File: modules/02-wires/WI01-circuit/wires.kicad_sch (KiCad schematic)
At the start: 24 parts, among them J1 MODULE Connector, SW1 SW_SPST, SW2 SW_SPST, SW3 SW_SPST, SW4 SW_SPST, SW5 SW_SPST, SW6 SW_SPST

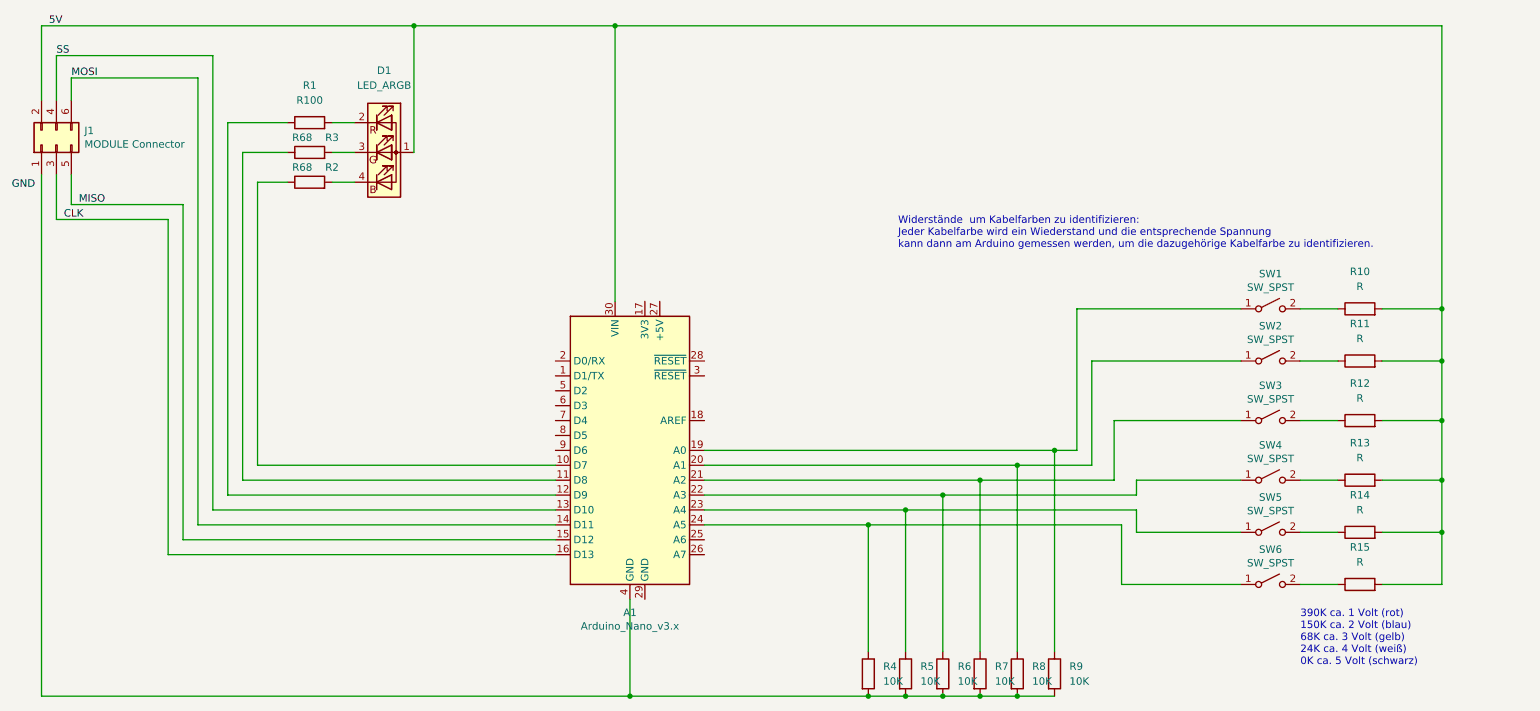
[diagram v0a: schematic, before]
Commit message: cleanup circuit
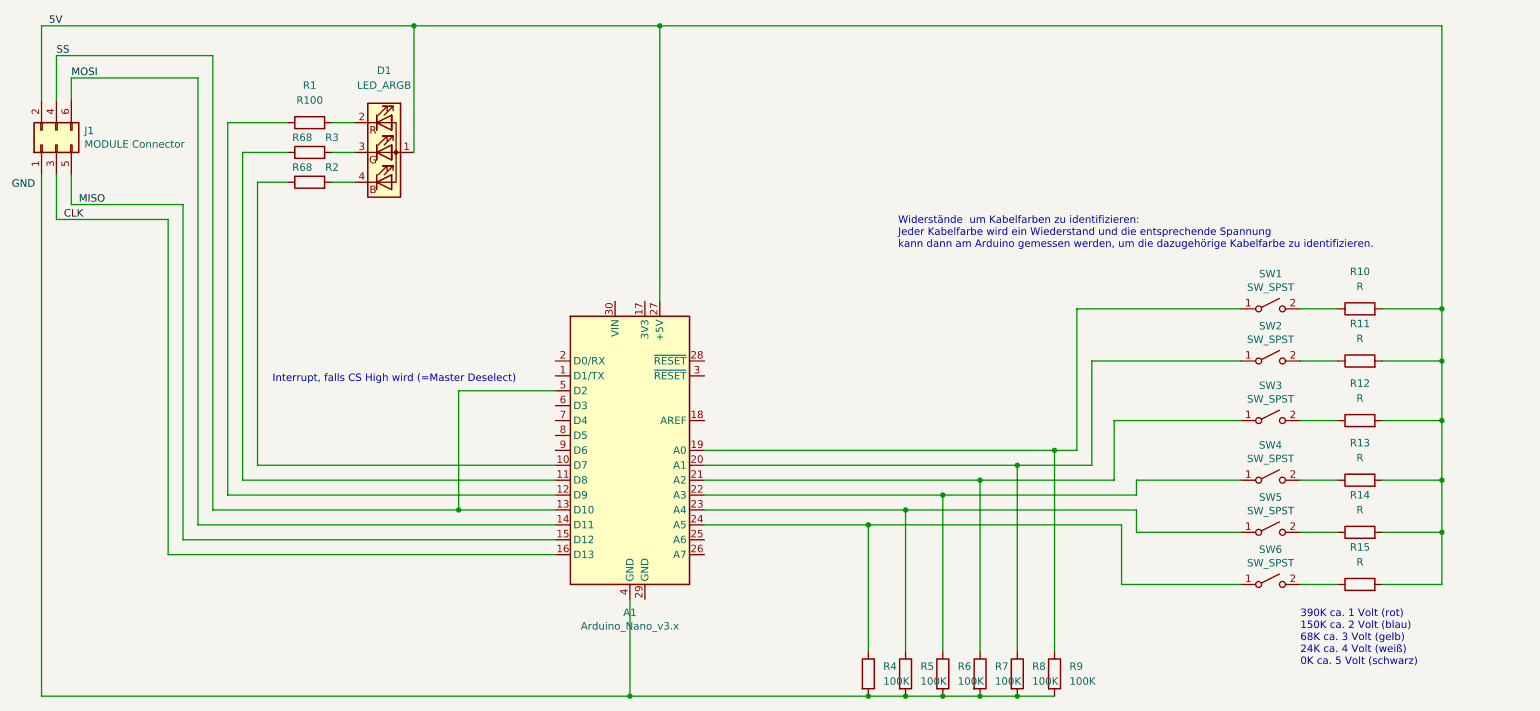
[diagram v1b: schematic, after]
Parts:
- R4, R5, R6, R7, R8, R9: value 10K -> 100K
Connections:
- net 5V: now also A1.27 (+5V); no longer A1.30 (VIN)
- net SS: now also A1.5 (D2)
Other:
- note added: "Interrupt, falls CS High wird (=Master Deselect)"
- title: (none) -> Schaltplan Modul Wires (02)
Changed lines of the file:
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@@
 (kicad_sch (version 20211123) (generator eeschema)
   (paper "A4")
+  (title_block
+    (title "Schaltplan Modul Wires (02)")
+    (date "14.12.2022")
+  )
   (junction (at 214.63 110.49) (diameter 0) (color 0 0 0 0)
   )
@@
   (junction (at 105.41 38.1) (diameter 0) (color 0 0 0 0)
   )
-  (junction (at 139.7 38.1) (diameter 0) (color 0 0 0 0)
-  )
   (junction (at 208.28 152.4) (diameter 0) (color 0 0 0 0)
   )
@@
   (junction (at 208.28 113.03) (diameter 0) (color 0 0 0 0)
   )
+  (junction (at 113.03 120.65) (diameter 0) (color 0 0 0 0)
+  )
   (junction (at 280.67 95.25) (diameter 0) (color 0 0 0 0)
   )
   (junction (at 182.88 152.4) (diameter 0) (color 0 0 0 0)
   )
+  (junction (at 147.32 38.1) (diameter 0) (color 0 0 0 0)
+  )
   (junction (at 189.23 152.4) (diameter 0) (color 0 0 0 0)
   )
@@
     (stroke (width 0) (type default) (color 0 0 0 0))
   )
-  (wire (pts (xy 71.12 120.65) (xy 129.54 120.65))
+  (wire (pts (xy 71.12 120.65) (xy 113.03 120.65))
     (stroke (width 0) (type default) (color 0 0 0 0))
   )
@@
     (stroke (width 0) (type default) (color 0 0 0 0))
   )
+  (wire (pts (xy 147.32 38.1) (xy 280.67 38.1))
+    (stroke (width 0) (type default) (color 0 0 0 0))
+  )
   (wire (pts (xy 280.67 86.36) (xy 280.67 95.25))
     (stroke (width 0) (type default) (color 0 0 0 0))
@@
     (stroke (width 0) (type default) (color 0 0 0 0))
   )
+  (wire (pts (xy 147.32 85.09) (xy 147.32 38.1))
+    (stroke (width 0) (type default) (color 0 0 0 0))
+  )
   (wire (pts (xy 46.99 50.8) (xy 46.99 46.99))
     (stroke (width 0) (type default) (color 0 0 0 0))
@@
     (stroke (width 0) (type default) (color 0 0 0 0))
   )
+  (wire (pts (xy 113.03 120.65) (xy 113.03 100.33))
+    (stroke (width 0) (type default) (color 0 0 0 0))
+  )
   (wire (pts (xy 142.24 152.4) (xy 142.24 135.89))
     (stroke (width 0) (type default) (color 0 0 0 0))
@@
     (stroke (width 0) (type default) (color 0 0 0 0))
   )
-  (wire (pts (xy 139.7 38.1) (xy 280.67 38.1))
-    (stroke (width 0) (type default) (color 0 0 0 0))
-  )
   (wire (pts (xy 201.93 115.57) (xy 224.79 115.57))
     (stroke (width 0) (type default) (color 0 0 0 0))
@@
     (stroke (width 0) (type default) (color 0 0 0 0))
   )
-  (wire (pts (xy 105.41 38.1) (xy 139.7 38.1))
+  (wire (pts (xy 113.03 100.33) (xy 129.54 100.33))
+    (stroke (width 0) (type default) (color 0 0 0 0))
+  )
+  (wire (pts (xy 113.03 120.65) (xy 129.54 120.65))
     (stroke (width 0) (type default) (color 0 0 0 0))
   )
@@
     (stroke (width 0) (type default) (color 0 0 0 0))
   )
+  (wire (pts (xy 105.41 38.1) (xy 147.32 38.1))
+    (stroke (width 0) (type default) (color 0 0 0 0))
+  )
   (wire (pts (xy 214.63 110.49) (xy 218.44 110.49))
     (stroke (width 0) (type default) (color 0 0 0 0))
@@
   )
   (wire (pts (xy 154.94 123.19) (xy 182.88 123.19))
-    (stroke (width 0) (type default) (color 0 0 0 0))
-  )
-  (wire (pts (xy 139.7 38.1) (xy 139.7 85.09))
     (stroke (width 0) (type default) (color 0 0 0 0))
   )
@@
   (text "390K ca. 1 Volt (rot)\n150K ca. 2 Volt (blau)\n68K ca. 3 Volt (gelb)\n24K ca. 4 Volt (weiß)\n0K ca. 5 Volt (schwarz)"
     (at 256.54 147.32 0)
+    (effects (font (size 1.27 1.27)) (justify left bottom))
+  )
+  (text "Interrupt, falls CS High wird (=Master Deselect)\n" (at 81.28 99.06 0)
     (effects (font (size 1.27 1.27)) (justify left bottom))
   )
@@
       (effects (font (size 1.27 1.27)) (justify left))
     )
-    (property "Value" "10K" (id 1) (at 210.82 149.8599 0)
+    (property "Value" "100K" (id 1) (at 210.82 149.8599 0)
       (effects (font (size 1.27 1.27)) (justify left))
     )
@@
       (effects (font (size 1.27 1.27)) (justify left))
     )
-    (property "Value" "10K" (id 1) (at 191.77 149.8599 0)
+    (property "Value" "100K" (id 1) (at 191.77 149.8599 0)
       (effects (font (size 1.27 1.27)) (justify left))
     )
@@
       (effects (font (size 1.27 1.27)) (justify left))
     )
-    (property "Value" "10K" (id 1) (at 185.42 149.8599 0)
+    (property "Value" "100K" (id 1) (at 185.42 149.8599 0)
       (effects (font (size 1.27 1.27)) (justify left))
     )
@@
       (effects (font (size 1.27 1.27)) (justify left))
     )
-    (property "Value" "10K" (id 1) (at 198.12 149.8599 0)
+    (property "Value" "100K" (id 1) (at 198.12 149.8599 0)
       (effects (font (size 1.27 1.27)) (justify left))
     )
@@
       (effects (font (size 1.27 1.27)) (justify left))
     )
-    (property "Value" "10K" (id 1) (at 217.17 149.8599 0)
+    (property "Value" "100K" (id 1) (at 217.17 149.8599 0)
       (effects (font (size 1.27 1.27)) (justify left))
     )
@@
       (effects (font (size 1.27 1.27)) (justify left))
     )
-    (property "Value" "10K" (id 1) (at 204.47 149.8599 0)
+    (property "Value" "100K" (id 1) (at 204.47 149.8599 0)
       (effects (font (size 1.27 1.27)) (justify left))
     )
@@
     )
     (path "/30915464-27f4-4a41-b71a-1deb31c47c01"
-      (reference "R4") (unit 1) (value "10K") (footprint "")
+      (reference "R4") (unit 1) (value "100K") (footprint "")
     )
     (path "/2beac67b-5d6c-4b22-9d70-82383f9dccfe"
-      (reference "R5") (unit 1) (value "10K") (footprint "")
+      (reference "R5") (unit 1) (value "100K") (footprint "")
     )
     (path "/88b715c2-87b9-435f-b2c1-fa2e3da49bc4"
-      (reference "R6") (unit 1) (value "10K") (footprint "")
+      (reference "R6") (unit 1) (value "100K") (footprint "")
     )
     (path "/b7560c61-9e57-429a-8e9e-36bfc07b1c3a"
-      (reference "R7") (unit 1) (value "10K") (footprint "")
+      (reference "R7") (unit 1) (value "100K") (footprint "")
     )
     (path "/0d968b39-56bb-4fd6-9b7a-9fb3148c63e0"
-      (reference "R8") (unit 1) (value "10K") (footprint "")
+      (reference "R8") (unit 1) (value "100K") (footprint "")
     )
     (path "/abadfaa1-6e45-4f16-a4f4-6a0bdb3ef1b1"
-      (reference "R9") (unit 1) (value "10K") (footprint "")
+      (reference "R9") (unit 1) (value "100K") (footprint "")
     )
     (path "/45012517-bb09-44b5-a21d-61b3fec4b4ca"
